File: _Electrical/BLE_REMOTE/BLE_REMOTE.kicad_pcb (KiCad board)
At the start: 4 copper layers, 49.5 x 38.5 mm, 76 parts, among them J1 PGRM, J2 Conn_01x02_Pin, J3 USBC, J4 SWITCH, J8 Display, J9 Battery, Q1 BSS806NEH6327XTSA1, Q2 NPN, Q3 PMOS, SW1 SW_Push, SW3 SW_Push, U1 nRF52832-QFxx, U2 BQ24232RGTR, U3 MIC5528-3.3YMX-TR, U4 MCP65R41, U5 IRF7319TRPBF, U6 316040005, Y1 Crystal_GND24

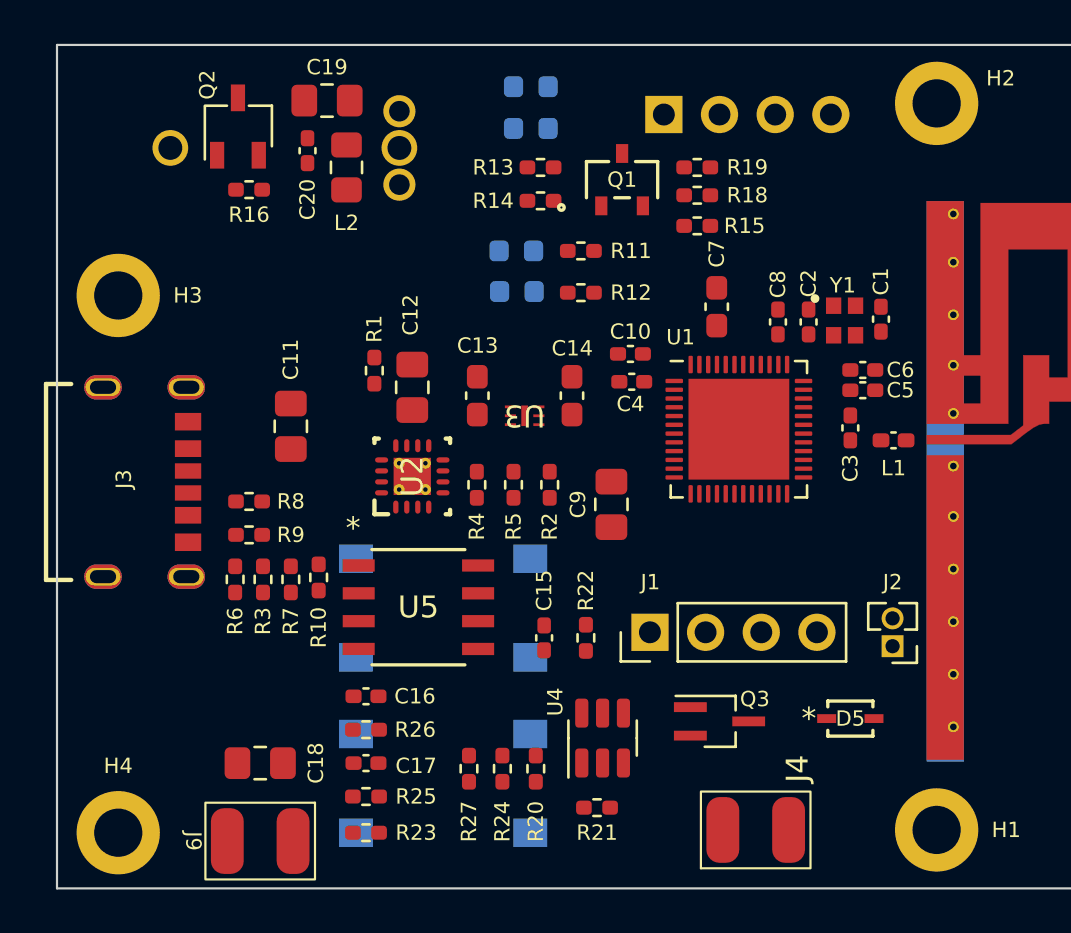
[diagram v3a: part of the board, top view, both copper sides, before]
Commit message: Finished initial PCB draft
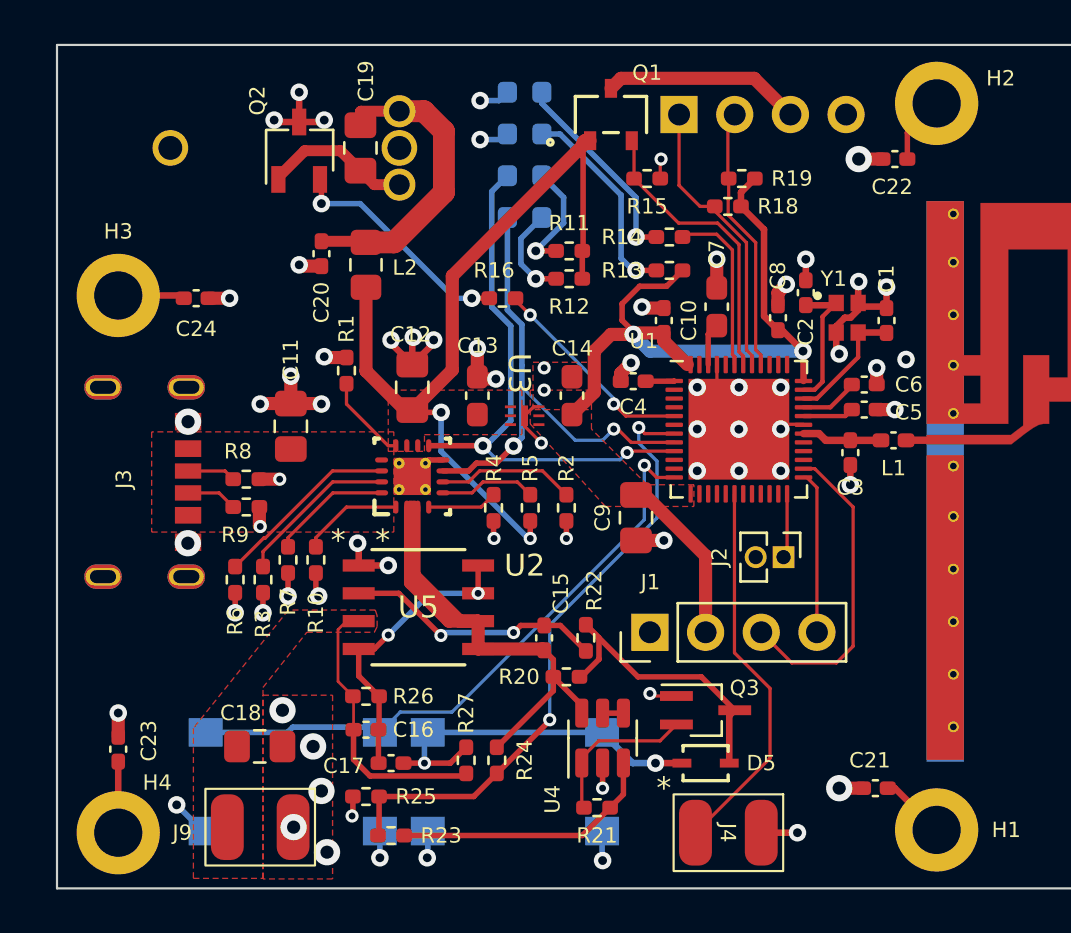
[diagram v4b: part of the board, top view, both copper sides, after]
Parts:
- added C21: 0.1uF, Capacitor_SMD:C_0402_1005Metric_Pad0.74x0.62mm_HandSolder, F.Cu at (163.1, 113.9)
- added C22: 0.1uF, Capacitor_SMD:C_0402_1005Metric_Pad0.74x0.62mm_HandSolder, F.Cu at (164.0, 85.2)
- added C23: 0.1uF, Capacitor_SMD:C_0402_1005Metric_Pad0.74x0.62mm_HandSolder, F.Cu at (128.5, 112.1)
- added C24: 0.1uF, Capacitor_SMD:C_0402_1005Metric_Pad0.74x0.62mm_HandSolder, F.Cu at (132.1, 91.6)
- moved R16 12.6 mm to (146.1, 91.6)
- moved SW3 10.5 mm to (136.5, 113.6)
- moved R13 7.53 mm to (153.7, 90.3)
- moved D5 6.91 mm to (155.3, 112.8)
- moved J2 6.42 mm to (158.9, 103.4), turned to -90 degrees
- moved R14 6.11 mm to (153.7, 88.8)
- moved C20 4.74 mm to (137.8, 89.5)
- moved L2 4.53 mm to (139.8, 90.0)
- moved R20 4.42 mm to (149.0, 108.8), turned to 0 degrees
- moved D1 3.45 mm to (147.1, 86.0)
- moved D2 3.40 mm to (147.1, 87.9)
- moved SW1 3.28 mm to (146.6, 113.6)
- moved R15 3.14 mm to (152.7, 86.1)
- moved Q1 3.01 mm to (151.0, 83.2)
- moved Q2 3.00 mm to (136.8, 84.8)
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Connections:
- net Net-(U2-TS) renamed /Power/BQ_TS
- C18 pad 2: /Power/Battery/BAT- -> GND
- H1 pad 1: GND -> Net-(C21-Pad2)
- H2 pad 1: GND -> Net-(C22-Pad2)
- H3 pad 1: GND -> Net-(C24-Pad2)
- H4 pad 1: GND -> Net-(C23-Pad2)
- J9 pad 1: /Power/Battery/BAT- -> GND
- U1 pad 12: unconnected-(U1-NFC2/P0.10-Pad12) -> BUTTON
- U1 pad 17: BUZZ -> unconnected-(U1-P0.14-Pad17)
- U1 pad 18: unconnected-(U1-P0.15-Pad18) -> SWITCH
- U1 pad 22: SWITCH -> unconnected-(U1-P0.19-Pad22)
- U1 pad 23: USER -> unconnected-(U1-P0.20-Pad23)
- U1 pad 27: BUTTON -> unconnected-(U1-P0.22-Pad27)
- U1 pad 28: TEST -> unconnected-(U1-P0.23-Pad28)
- U1 pad 37: DIS_SCL -> unconnected-(U1-P0.25-Pad37)
- U1 pad 38: DIS_SDA -> unconnected-(U1-P0.26-Pad38)
- U1 pad 39: DIS_EN -> unconnected-(U1-P0.27-Pad39)
- U1 pad 4: TEST_BAT -> unconnected-(U1-P0.02/AIN0-Pad4)
- U1 pad 40: unconnected-(U1-P0.28/AIN4-Pad40) -> DIS_SCL
- U1 pad 41: unconnected-(U1-P0.29/AIN5-Pad41) -> DIS_SDA
- U1 pad 42: unconnected-(U1-P0.30/AIN6-Pad42) -> DIS_EN
- U1 pad 43: unconnected-(U1-P0.31/AIN7-Pad43) -> USER
- U1 pad 5: unconnected-(U1-P0.03/AIN1-Pad5) -> BUZZ
- U1 pad 7: unconnected-(U1-P0.05/AIN3-Pad7) -> TEST_BAT
- U1 pad 8: CHG_N -> PGOOD_N
- U1 pad 9: PGOOD_N -> CHG_N
- U2 pad V: (no net) -> GND
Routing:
- net GND: track 0.00 -> 72.8 mm, vias 0 -> 70
- net VDD: track 0.00 -> 40.3 mm, vias 0 -> 2
- net VCC: track 0.00 -> 38.4 mm, vias 0 -> 2
- net TEST_BAT: track 0.00 -> 28.3 mm, vias 0 -> 2
- net BUTTON: track 0.00 -> 28.3 mm, vias 0 -> 1
- net /Power/Battery/VBAT: track 0.00 -> 26.3 mm
- net CHG_N: track 0.00 -> 25.2 mm, vias 0 -> 2
- net PGOOD_N: track 0.00 -> 24.0 mm, vias 0 -> 2
- net SWITCH: track 0.00 -> 17.5 mm
- net Net-(D5-K): track 0.00 -> 16.8 mm, vias 0 -> 2
- net /MCU/SWDIO: track 0.00 -> 14.4 mm
- net Net-(C19-Pad1): track 0.00 -> 14.2 mm
- net /Power/Battery/BAT_CTRL: track 0.00 -> 14.0 mm
- net Net-(U5-G2): track 0.00 -> 13.4 mm, vias 0 -> 2
- net DIS_EN: track 0.00 -> 13.4 mm
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- added copper zone on F.Cu, net +5V
- added copper zone on F.Cu, net /Power/Battery/BAT+
- added copper zone on F.Cu, net GND
- added copper zone on In1.Cu, net GND
- added copper zone on In2.Cu, net GND
- added copper zone on F.Cu, net VCC
- added copper zone on F.Cu, net VDD

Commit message: second iteration PCB layout
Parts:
- added J6: LED, _Parts:3pad_conn, B.Cu at (128.7, 113.4)
- moved D5 12.8 mm to (142.5, 113.5)
- moved R25 7.92 mm to (147.6, 115.7), turned to 0 degrees
- moved R23 6.92 mm to (147.6, 114.2)
- moved R22 6.48 mm to (145.7, 112.1), turned to 180 degrees
- moved SW3 5.50 mm to (141.4, 111.2), turned to 90 degrees
- moved C15 4.20 mm to (144.9, 110.0), turned to -90 degrees
- moved R27 4.10 mm to (140.5, 111.5), turned to 180 degrees
- moved C23 3.83 mm to (132.3, 112.8)
- moved R11 3.61 mm to (148.1, 86.0), turned to 0 degrees
- moved R12 3.49 mm to (147.0, 87.9), turned to 0 degrees
- moved H4 3.41 mm to (131.9, 116.1)
- moved R24 3.21 mm to (147.6, 110.0)
- moved R20 3.00 mm to (146.2, 110.0), turned to -90 degrees
- moved J9 2.98 mm to (136.8, 113.3)
- moved SW1 2.91 mm to (148.2, 111.2), turned to -90 degrees
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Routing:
- net TEST_BAT: track 28.3 -> 50.8 mm
- net GND: track 72.8 -> 58.0 mm, vias 70 -> 114
- net /Power/Battery/VBAT: track 26.3 -> 14.5 mm
- net +5V: track 0.00 -> 8.98 mm, vias 0 -> 8
- net Net-(U4-+): track 12.2 -> 5.25 mm
- net BUTTON: track 28.3 -> 21.8 mm
- net /Power/Battery/BAT+: track 12.8 -> 6.62 mm
- net VCC: track 38.4 -> 32.6 mm
- net Net-(D2-A): track 4.40 -> 1.65 mm
- net Net-(D1-A): track 5.29 -> 2.66 mm
- net SWITCH: track 17.5 -> 15.2 mm
- net Net-(U5-G1): track 11.8 -> 10.0 mm, vias 2 -> 0
- net /Power/Battery/BAT_CTRL: track 14.0 -> 15.6 mm
- net Net-(C19-Pad1): track 14.2 -> 13.5 mm
- net Net-(Q3-G): track 7.02 -> 7.69 mm
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- added copper zone on B.Cu, net +5V
- added copper zone on B.Cu, net GND

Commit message: finished initial PCB draft
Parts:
- moved SW1 9.86 mm to (138.4, 111.5), turned to 90 degrees
- moved SW3 6.81 mm to (148.2, 111.5)
- moved J9 1.41 mm to (137.4, 114.6)
- moved R6 0.84 mm to (133.9, 103.3)
- moved R3 0.79 mm to (135.2, 103.3)
- moved J4 0.67 mm to (156.1, 114.9)
- moved C18 0.58 mm to (137.0, 110.0)
- moved C9 0.41 mm to (151.7, 101.6)
- moved H4 0.38 mm to (132.3, 116.1)
- moved J8 0.32 mm to (154.0, 82.9)
- moved C4 0.28 mm to (151.7, 95.4)
- moved C7 0.22 mm to (155.7, 91.8)
- moved R10 0.18 mm to (137.6, 103.3)
- moved R7 0.18 mm to (136.4, 103.3)
- moved C10 0.15 mm to (153.4, 92.4)
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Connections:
- J6 pad 2: TEST_BAT -> LED_D
- U1 pad 11: unconnected-(U1-NFC1/P0.09-Pad11) -> LED_D
- U1 pad 12: BUTTON -> unconnected-(U1-NFC2/P0.10-Pad12)
- U1 pad 15: unconnected-(U1-P0.12-Pad15) -> BUTTON
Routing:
- net LED_D: track 0.00 -> 29.8 mm, vias 0 -> 1
- net TEST_BAT: track 50.8 -> 24.2 mm
- net BUTTON: track 21.8 -> 17.3 mm
- net Net-(D5-K): track 17.2 -> 13.5 mm
- net GND: track 58.0 -> 55.8 mm, vias 114 -> 132
- net VCC: track 32.6 -> 32.0 mm
- net /Power/BQ_ITERM: track 7.05 -> 6.47 mm
- net VDD: track 40.3 -> 40.9 mm
- net /Power/Battery/VBAT: vias 0 -> 1

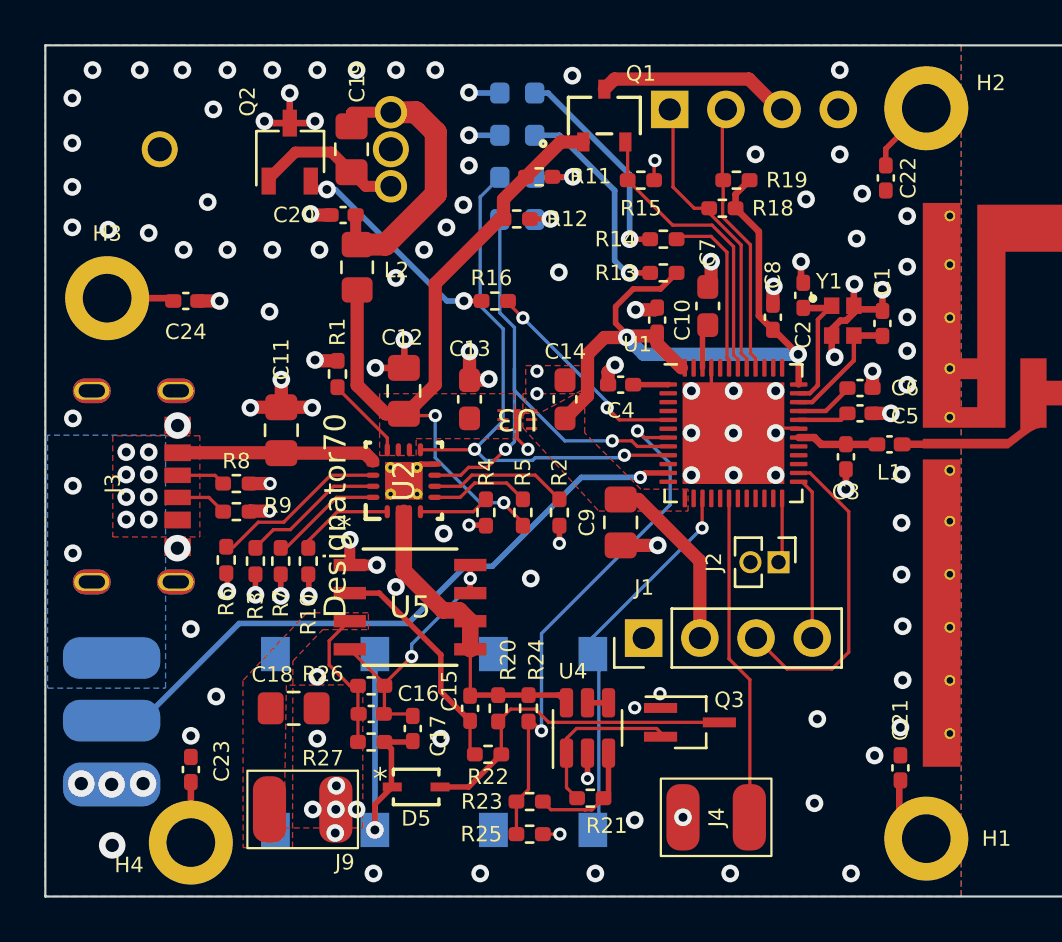
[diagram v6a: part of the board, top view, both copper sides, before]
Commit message: JLCPCB parts selected
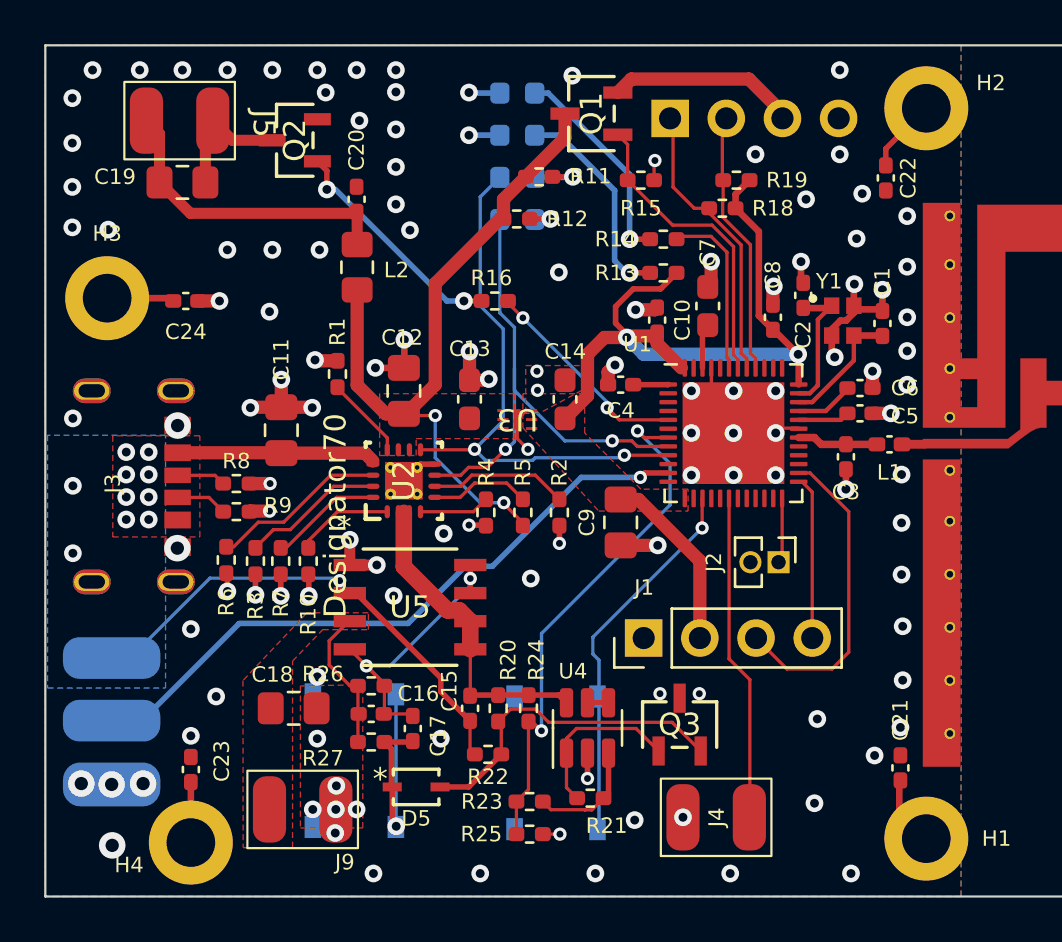
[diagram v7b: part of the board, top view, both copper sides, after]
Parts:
- removed U6: 316040005, _Parts:316040005
- added J5: BUZZER, _Parts:2pad_conn_sm, F.Cu at (131.8, 83.4)
- Q1: footprint _Parts:PG-SOT23-3-5_INF -> _Parts:SOT-23-3L_AOS
- Q2: footprint Package_TO_SOT_SMD:TSOT-23 -> _Parts:TRAN_SS8050-G_CIP
- Q3: footprint Package_TO_SOT_SMD:SOT-323_SC-70_Handsoldering -> _Parts:SOT-23-3L_AOS
- R24: value 173k -> 178k
- SW1, SW3: footprint Button_Switch_SMD:SW_Push_1P1T_NO_6x6mm_H9.5mm -> _Parts:SW_TS-1187A-B-A-B
- moved C19 7.79 mm to (131.9, 86.2), turned to 0 degrees
- moved SW1 1.57 mm to (139.7, 112.3)
- moved SW3 1.11 mm to (148.8, 112.4)
- moved C20 0.94 mm to (139.8, 87.0), turned to 90 degrees
- moved Q1 0.59 mm to (150.4, 83.1), turned to 90 degrees
- moved Q2 0.58 mm to (137.0, 84.3)
- moved Q3 0.48 mm to (154.4, 110.7)
- moved J8 0.40 mm to (154.0, 83.3)
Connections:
- C15 pad 2: Net-(U5-G1) -> +5V
- C19 pad 2: Net-(Q2-C) -> Net-(J5-Pin_1)
- Q1 pad 1: VCC -> DIS_EN
- Q1 pad 2: DIS_EN -> /Peripherals/DIS_PWR
- Q1 pad 3: /Peripherals/DIS_PWR -> VCC
- Q2 pad 1: Net-(Q2-C) -> Net-(Q2-Pad1)
- Q2 pad 2: Net-(Q2-B) -> GND
- Q2 pad 3: GND -> Net-(J5-Pin_1)
- Q3 pad 1: GND -> Net-(Q3-G)
- Q3 pad 2: Net-(Q3-G) -> /Power/Battery/BAT_CTRL
- Q3 pad 3: /Power/Battery/BAT_CTRL -> GND
- R16 pad 2: Net-(Q2-B) -> Net-(Q2-Pad1)
- R22 pad 2: Net-(U5-G1) -> +5V
- U5 pad 2: Net-(U5-G1) -> +5V
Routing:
- net +5V: track 8.98 -> 31.4 mm, vias 8 -> 9
- net Net-(Q2-Pad1): track 0.00 -> 10.5 mm, vias 0 -> 2
- net Net-(U5-G1): track 10.4 -> 0.00 mm
- net Net-(Q2-B): track 9.97 -> 0.00 mm, vias 2 -> 0
- net Net-(Q2-C): track 6.77 -> 0.00 mm
- net Net-(J5-Pin_1): track 0.00 -> 5.99 mm
- net GND: track 55.8 -> 51.2 mm, vias 132 -> 126
- net Net-(D5-K): track 13.5 -> 11.3 mm
- net Net-(U5-G2): track 13.3 -> 14.6 mm
- net Net-(J5-Pin_2): track 13.5 -> 14.0 mm
- net /Peripherals/DIS_PWR: track 9.06 -> 8.51 mm
- net /Power/Battery/BAT_CTRL: track 15.6 -> 15.1 mm
- net /Power/Battery/VBAT: track 14.5 -> 14.4 mm, vias 1 -> 0

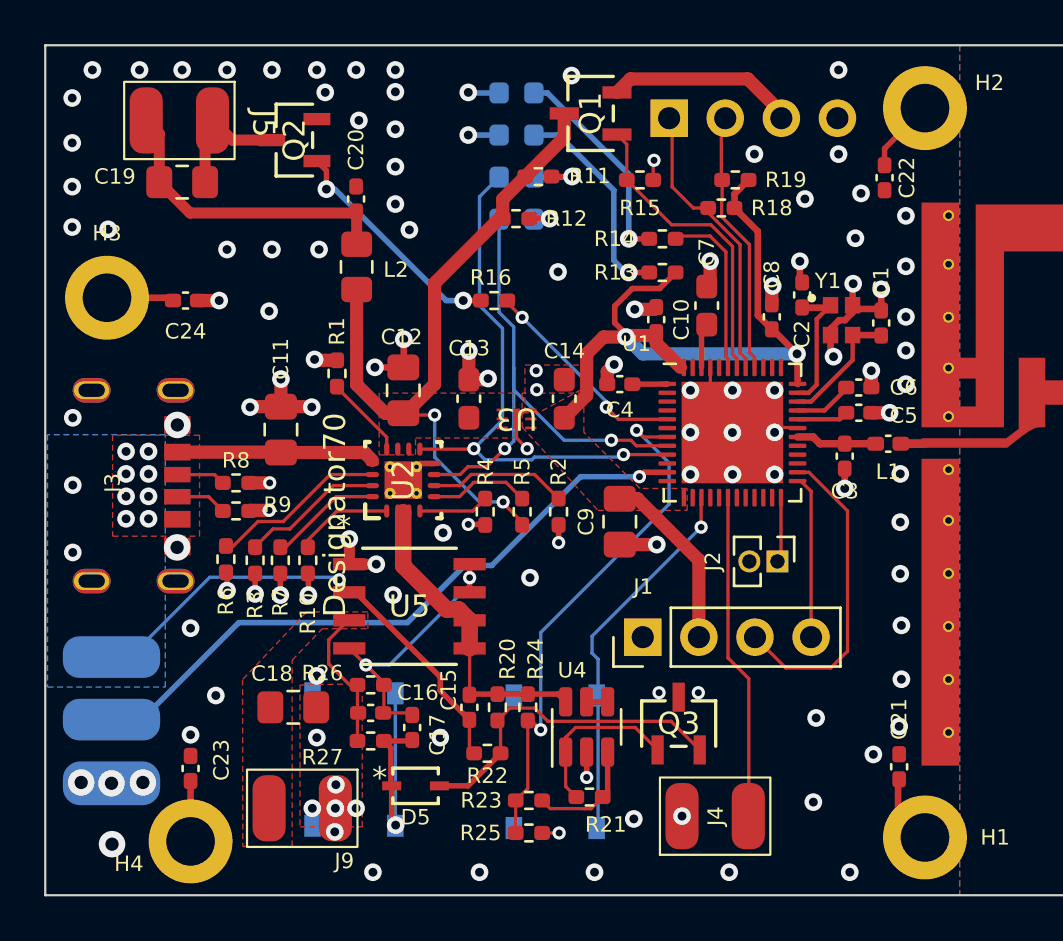
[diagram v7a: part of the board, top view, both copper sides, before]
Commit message: Adjusted components and changed buttons
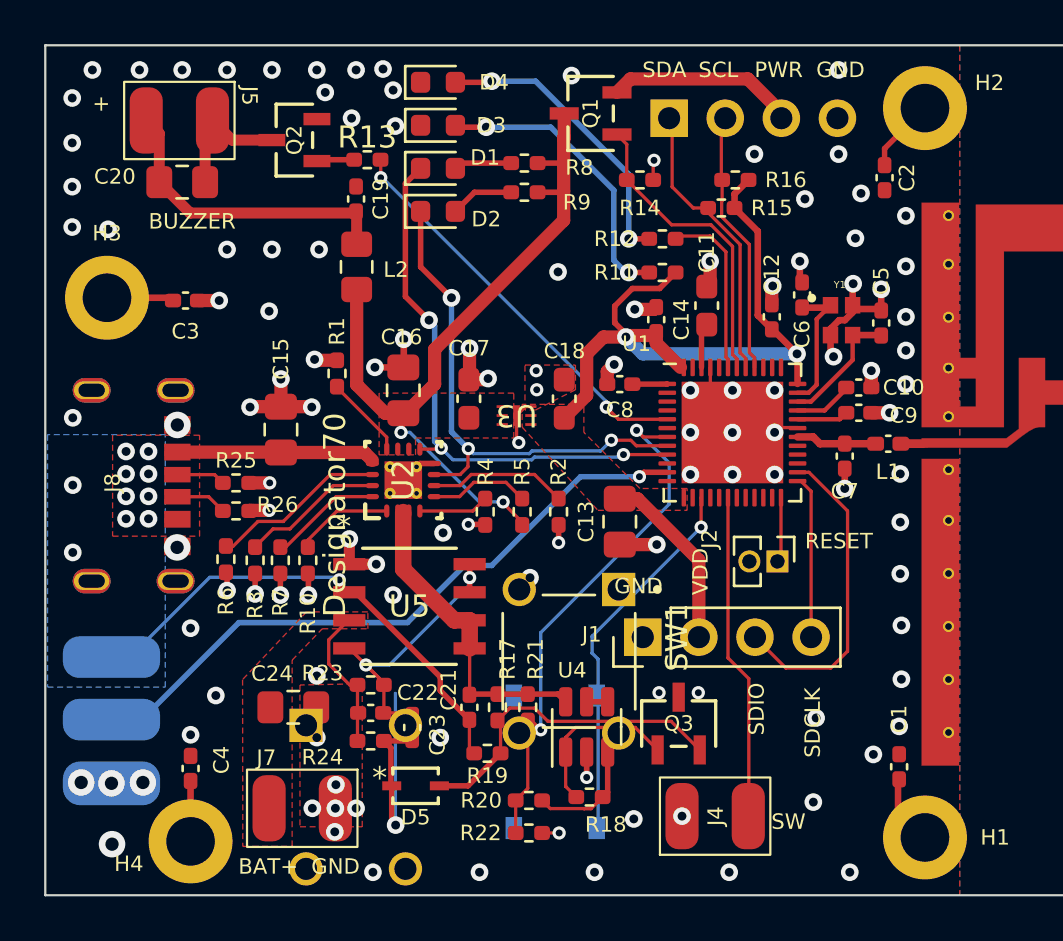
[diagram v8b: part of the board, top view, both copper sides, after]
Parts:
- removed the R16 at (146.1, 91.6)
- added R13: 220, Resistor_SMD:R_0402_1005Metric_Pad0.72x0.64mm_HandSolder, F.Cu at (140.3, 85.2)
- added SW1: SW_Push, _Parts:SW_TS02-66-120-BK-260-LCR-D, F.Cu at (149.4, 107.9)
- D1, D2, D3, D4: moved to F.Cu
- SW2: renamed from SW1; footprint _Parts:SW_TS-1187A-B-A-B -> _Parts:SW_TS02-66-120-BK-260-LCR-D
- moved D4 3.59 mm to (143.5, 81.7)
- moved D3 3.58 mm to (143.5, 83.6)
- moved D1 3.58 mm to (143.5, 85.6)
- moved D2 3.57 mm to (143.5, 87.5)
- moved SW2 1.70 mm to (139.8, 114.0), turned to -90 degrees
- moved R9 1.25 mm to (147.4, 86.7), turned to 180 degrees
- moved R8 0.88 mm to (147.4, 85.3), turned to 180 degrees
- moved U3 0.15 mm to (147.1, 96.8)
- renumbered C21 to C1, C6 to C10, C7 to C11, C8 to C12, C9 to C13, C10 to C14, C11 to C15, C12 to C16, C13 to C17, C14 to C18, C20 to C19, C22 to C2, C19 to C20, C15 to C21, C16 to C22, C17 to C23, C18 to C24, C24 to C3, C23 to C4, C1 to C5, C2 to C6, C3 to C7, C4 to C8, C5 to C9, J6 to J3, J8 to J6, J9 to J7, J3 to J8, R13 to R11, R14 to R12, R15 to R14, R18 to R15, R19 to R16, R20 to R17, R21 to R18, R22 to R19, R23 to R20, R24 to R21, R25 to R22, R26 to R23, R27 to R24, R8 to R25, R9 to R26, R11 to R8, R12 to R9
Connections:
- net Net-(J5-Pin_2) renamed /Peripherals/BUZZ+
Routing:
- net Net-(Q2-Pad1): track 10.5 -> 1.71 mm, vias 2 -> 0
- net BUZZ: track 9.67 -> 18.5 mm
- net Net-(D4-A): track 9.67 -> 13.5 mm, vias 1 -> 2
- net Net-(D3-A): track 9.66 -> 13.4 mm, vias 1 -> 2
- net GND: track 51.2 -> 48.2 mm, vias 126 -> 117
- net VCC: track 32.3 -> 34.2 mm
- net Net-(D2-A): track 1.65 -> 2.88 mm, vias 1 -> 0
- net CHG_N: track 25.1 -> 25.2 mm, vias 2 -> 3
- net PGOOD_N: vias 2 -> 3
- net Net-(D1-A): track 2.66 -> 2.62 mm, vias 1 -> 0
- net unconnected-(SW2-Pad4): vias 0 -> 1
- net unconnected-(SW2-Pad1): vias 0 -> 1
- net unconnected-(SW1-Pad3): vias 0 -> 1
- net unconnected-(SW1-Pad2): vias 0 -> 1
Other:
- board text added: "+"
- board text added: "5V"
- board text added: "BAT+"
- board text added: "BUZZER"
- board text added: "D+"
- board text added: "GND"
- board text added: "PWR"
- board text added: "RESET"
- board text added: "SCL"
- board text added: "SDA"
- board text added: "SDCLK"
- board text added: "SDIO"
- board text added: "SW"
- board text added: "VDD"
